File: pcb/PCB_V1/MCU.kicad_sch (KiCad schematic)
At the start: 19 parts, among them J201 UART / 3V3 logic, SW201 RESET, SW202 BOOT, U201 ESP32-WROOM-32E-N4

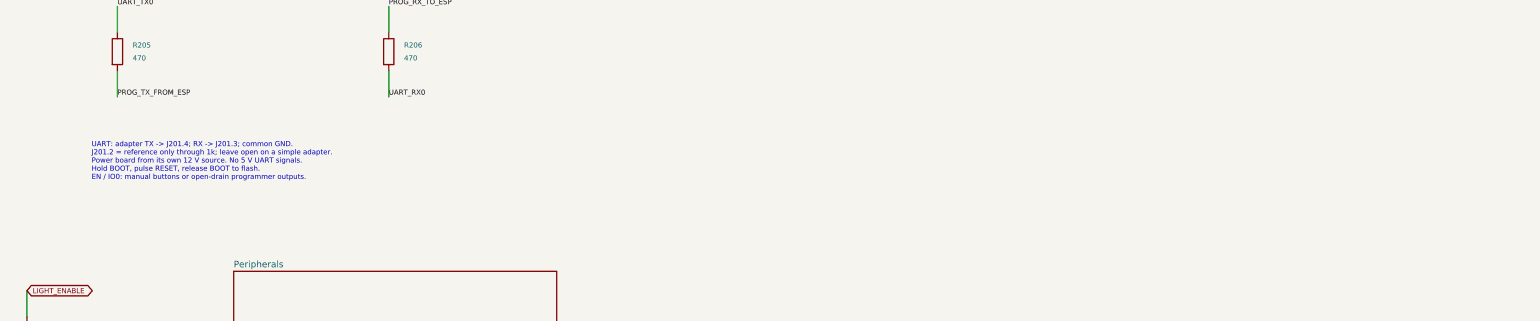
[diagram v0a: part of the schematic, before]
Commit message: pcb: move board to 24 V input with 12 V aux buck and merged LED bar channel
Revision 0.14 of PCB_V1 (see pcb/PCB_V1/REDESIGN_24V.md):
- 24 V input on keyed XT60PW-M (pin 1 GND, pin 2 +24V); LM74700, input
  MOSFET and F901 removed; SMBJ26CA TVS; 220 uF/50 V bulk
- ATM mini-blade fuses in XF-508P-B-B holders: F902 10 A loads, F903 7.5 A LED
- new LMR16020 24 V -> 12 V aux buck (500 kHz) feeding PC fans, the
  UCC27524A heater gate driver and the TPS54202 3.3 V buck; TPS70950 removed
- heater and pump on 24 V: SMBJ30A drain TVS, AO3422 + SS36 pump stage
- LED CH1 panel keeps SRP1770TA/0.027 R/1k, switch now CSD19534Q5A;
  CH2 drives both identical bars in parallel (J721 || J731, 0.40 R);
  third AL8853 channel removed
- TS-1187A buttons, DORABO/KANGNEX terminals
- project library: LMR16020 and CSD19534Q5A symbols, TI DQJ and XF-508P
  footprints
- verify_netlist.py / verify_board.py / analyze_*.py updated for 24 V;
  new sync_board.py updates the unrouted staging board from the netlist
- ERC 0/0; netlist, board and sizing checks pass; DRC only the 12 known
  ESP32 drill sizes plus unrouted connections; 163 components

Co-Authored-By: Claude Opus 5.5 <noreply@anthropic.com>
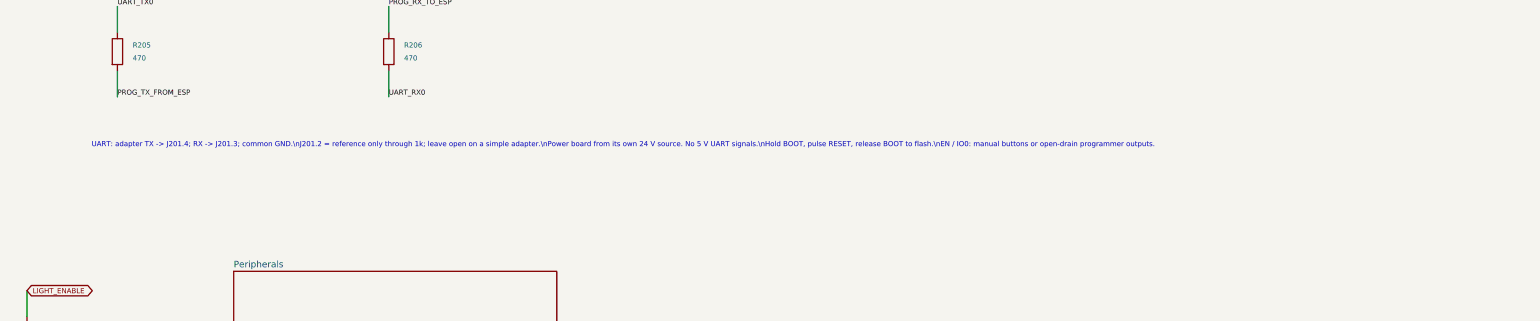
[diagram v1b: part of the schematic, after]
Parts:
- SW201, SW202: footprint Button_Switch_SMD:SW_SPST_TL3342 -> Button_Switch_SMD:SW_Push_1P1T_XKB_TS-1187A; LCSC (none) -> C318884; MPN (none) -> TS-1187A-B-A-B; Manufacturer (none) -> XKB Connection
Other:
- note added: "UART: adapter TX -> J201.4; RX -> J201.3; common GND.\nJ201.2 = reference only through 1k; leave open on a simple adapter.\nPower board from its own 24 V source. No 5 V UART signals.\nHold BOOT, pulse RESET, release BOOT to flash.\nEN / IO0: manual buttons or open-drain programmer outputs."
- note removed: "UART: adapter TX -> J201.4; RX -> J201.3; common GND. J201.2 = reference only through 1k; leave open on a simple adapter. Power board from its own 12 V source. No 5 V UART signals. Hold BOOT, pulse RESET, release BOOT to flash. EN / IO0: manual buttons or open-drain programmer outputs."
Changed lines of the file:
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@@
 		(comment 1 "Draft: input protection and LED drivers pending")
 	)
-	(text "UART: adapter TX -> J201.4; RX -> J201.3; common GND.\nJ201.2 = reference only through 1k; leave open on a simple adapter.\nPower board from its own 12 V source. No 5 V UART signals.\nHold BOOT, pulse RESET, release BOOT to flash.\nEN / IO0: manual buttons or open-drain programmer outputs."
+	(text "UART: adapter TX -> J201.4; RX -> J201.3; common GND.\\nJ201.2 = reference only through 1k; leave open on a simple adapter.\\nPower board from its own 24 V source. No 5 V UART signals.\\nHold BOOT, pulse RESET, release BOOT to flash.\\nEN / IO0: manual buttons or open-drain programmer outputs."
 		(exclude_from_sim no)
 		(at 177.8 121.92 0)
@@
 			)
 		)
-		(property "Footprint" "Button_Switch_SMD:SW_SPST_TL3342"
+		(property "Footprint" "Button_Switch_SMD:SW_Push_1P1T_XKB_TS-1187A"
 			(at 236.22 45.72 0)
 			(hide yes)
@@
 					(unit 1)
 				)
+			)
+		)
+		(property "LCSC" "C318884"
+			(at 236.22 45.72 0)
+			(effects
+				(font
+					(size 1 1)
+				)
+				(hide yes)
+				(justify left)
+			)
+		)
+		(property "MPN" "TS-1187A-B-A-B"
+			(at 236.22 45.72 0)
+			(effects
+				(font
+					(size 1 1)
+				)
+				(hide yes)
+				(justify left)
+			)
+		)
+		(property "Manufacturer" "XKB Connection"
+			(at 236.22 45.72 0)
+			(effects
+				(font
+					(size 1 1)
+				)
+				(hide yes)
+				(justify left)
 			)
 		)
@@
 			)
 		)
-		(property "Footprint" "Button_Switch_SMD:SW_SPST_TL3342"
+		(property "Footprint" "Button_Switch_SMD:SW_Push_1P1T_XKB_TS-1187A"
 			(at 182.88 45.72 0)
 			(hide yes)
@@
 			)
 		)
+		(property "LCSC" "C318884"
+			(at 182.88 45.72 0)
+			(effects
+				(font
+					(size 1 1)
+				)
+				(hide yes)
+				(justify left)
+			)
+		)
+		(property "MPN" "TS-1187A-B-A-B"
+			(at 182.88 45.72 0)
+			(effects
+				(font
+					(size 1 1)
+				)
+				(hide yes)
+				(justify left)
+			)
+		)
+		(property "Manufacturer" "XKB Connection"
+			(at 182.88 45.72 0)
+			(effects
+				(font
+					(size 1 1)
+				)
+				(hide yes)
+				(justify left)
+			)
+		)
